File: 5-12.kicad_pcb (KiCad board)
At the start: 2 copper layers, 136 parts, among them SW1 SW_Push, U1 ATmega32U4-AU, Y1 16MHz

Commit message: Partially placed diodes
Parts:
- moved D1 258.6 mm to (28.6, 83.3), turned to 90 degrees
- moved D2 257.8 mm to (29.4, 102.4), turned to 90 degrees
- moved D3 239.4 mm to (29.4, 121.5), turned to 90 degrees
- moved D4 227.8 mm to (29.4, 140.6), turned to 90 degrees
- moved D7 226.8 mm to (48.4, 102.4), turned to 90 degrees
- moved D11 223.2 mm to (67.5, 83.3), turned to 90 degrees
- moved D6 218.9 mm to (48.4, 83.3), turned to 90 degrees
- moved D5 214.1 mm to (29.4, 159.6), turned to 90 degrees
- moved F1 206.3 mm to (162.7, 57.9)
- moved D16 205.3 mm to (86.5, 83.3), turned to 90 degrees
- moved D26 202.8 mm to (124.6, 83.3), turned to 90 degrees
- moved USB1 200.6 mm to (143.5, 55.5), turned to 270 degrees
- moved D21 197.7 mm to (105.6, 83.3), turned to 90 degrees
- moved D13 185.0 mm to (67.5, 121.5), turned to 90 degrees
- moved D27 177.6 mm to (124.6, 102.5), turned to 90 degrees
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
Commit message: swapped MX footprints for NOLED version
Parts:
- MX1, MX10, MX11, MX12, MX13, MX14, MX15, MX16, MX17, MX18, MX19, MX2, MX20, MX21, MX22, MX23, MX24, MX25, MX26, MX27, MX28, MX29, MX3, MX31, MX32, MX33, MX34, MX36, MX37, MX38, MX39, MX4, MX40, MX41, MX42, MX43, MX44, MX45, MX46, MX47, MX48, MX49, MX5, MX50, MX51, MX52, MX53, MX54, MX55, MX56, MX57, MX58, MX59, MX6, MX60, MX7, MX8, MX9: footprint MX_Only:MXOnly-1U -> MX_Only:MXOnly-1U-NoLED
- MX30, MX35: footprint MX_Only:MXOnly-2U -> MX_Only:MXOnly-2U-ReversedStabilizers-NoLED

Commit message: initial, normal diode placement done
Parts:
- moved D12 213.0 mm to (67.5, 102.3), turned to 90 degrees
- moved D56 211.5 mm to (277.0, 83.4), turned to 90 degrees
- moved D51 209.3 mm to (258.0, 83.4), turned to 90 degrees
- moved D57 200.5 mm to (277.0, 102.5), turned to 90 degrees
- moved D58 195.4 mm to (277.0, 121.5), turned to 90 degrees
- moved D17 193.7 mm to (86.5, 102.5), turned to 90 degrees
- moved D41 190.8 mm to (219.9, 83.4), turned to 90 degrees
- moved D59 189.2 mm to (277.0, 140.5), turned to 90 degrees
- moved D18 187.4 mm to (86.5, 121.4), turned to 90 degrees
- moved D22 184.3 mm to (105.6, 102.5), turned to 90 degrees
- moved D31 182.8 mm to (181.8, 83.3), turned to 90 degrees
- moved D42 182.6 mm to (219.9, 102.5), turned to 90 degrees
- moved D46 181.7 mm to (238.9, 83.4), turned to 90 degrees
- moved D8 176.7 mm to (48.4, 121.4), turned to 90 degrees
- moved D48 172.9 mm to (238.9, 121.5), turned to 90 degrees
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
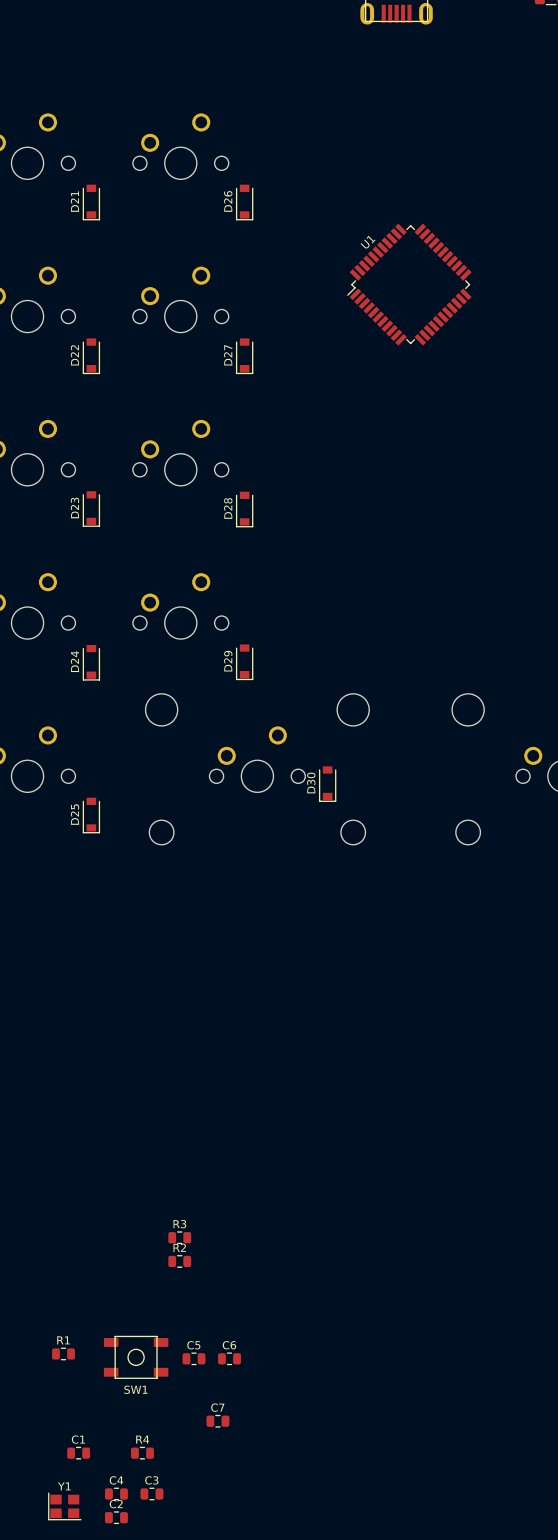
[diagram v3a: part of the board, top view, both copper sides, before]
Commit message: Completed initial layout for MCU zone
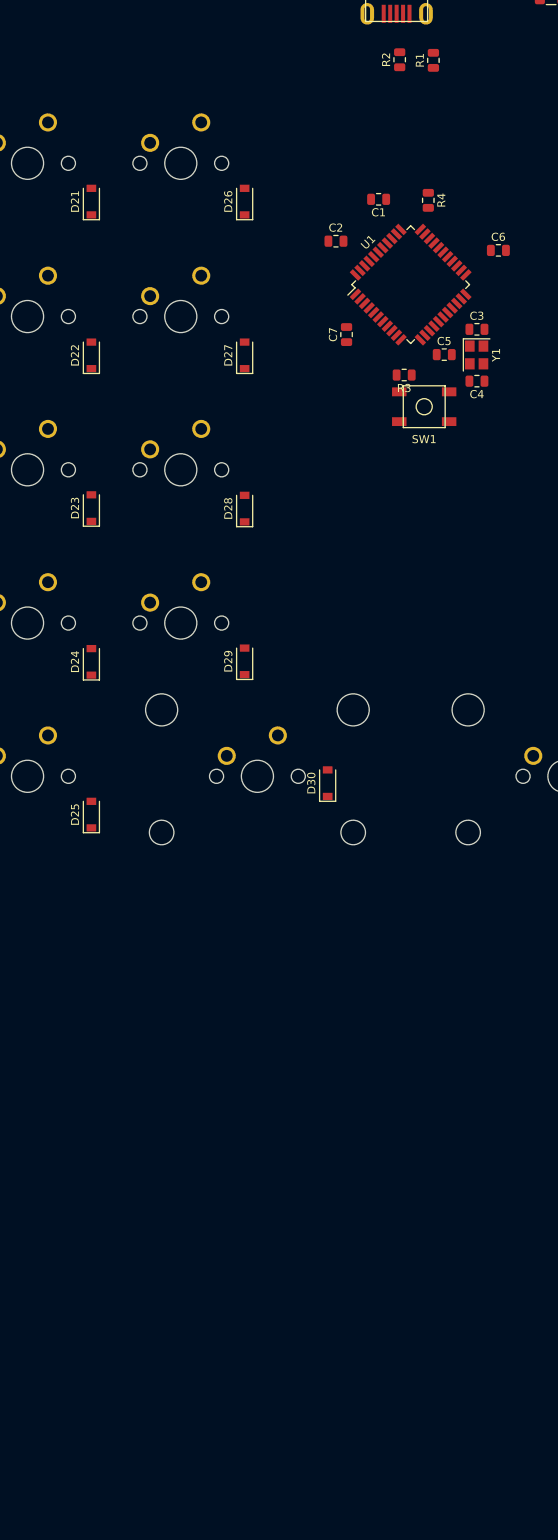
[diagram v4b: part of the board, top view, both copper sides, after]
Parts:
- moved R1 167.2 mm to (148.1, 65.8), turned to 90 degrees
- moved C2 161.0 mm to (136.0, 88.3)
- moved C1 160.3 mm to (141.3, 83.1), turned to 180 degrees
- moved R4 159.7 mm to (147.4, 83.2), turned to 270 degrees
- moved Y1 152.0 mm to (153.5, 102.4), turned to 270 degrees
- moved R2 151.9 mm to (143.9, 65.7), turned to 90 degrees
- moved C3 150.3 mm to (153.5, 99.2)
- moved C4 145.4 mm to (153.5, 105.7), turned to 180 degrees
- moved C6 141.8 mm to (156.2, 89.4)
- moved C7 136.0 mm to (137.3, 99.9), turned to 90 degrees
- moved C5 128.6 mm to (149.4, 102.4)
- moved SW1 123.5 mm to (146.9, 108.8)
- moved R3 110.8 mm to (144.4, 104.9), turned to 180 degrees

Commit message: Initial usb placement
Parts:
- moved R1 17.5 mm to (165.5, 66.6)
- moved R2 17.5 mm to (161.4, 66.5)
- moved USB1 15.3 mm to (145.7, 70.6)
- moved F1 4.36 mm to (159.7, 61.1)
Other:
- board outline added: 266.7 x 95.2 mm
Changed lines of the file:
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@@
   (general
     (thickness 1.6)
-    (drawings 0)
+    (drawings 8)
     (tracks 0)
     (zones 0)
@@
   )
   (module random-keyboard-parts:Molex-0548190589 (layer F.Cu)
-    (at 143.51 55.499 270)
+    (at 145.70625 70.64375 270)
     (attr smd)
     (fp_text reference USB1 (at 2.032 0) (layer F.SilkS)
@@
   )
   (module Resistor_SMD:R_0805_2012Metric (layer F.Cu)
-    (at 143.891 65.7075 90)
+    (at 161.3535 66.50125 90)
     (descr "Resistor SMD 0805 (2012 Metric), square (rectangular) end terminal, IPC_7351 nominal, (Body size source: https://docs.google.com/spreadsheets/d/1BsfQQcO9C6DZCsRaXUlFlo91Tg2WpOkGARC1WS5S8t0/edit?usp=sharing), generated with kicad-footprint-generator")
     (tags resistor)
@@
   )
   (module Resistor_SMD:R_0805_2012Metric (layer F.Cu)
-    (at 148.082 65.786 90)
+    (at 165.5445 66.57975 90)
     (descr "Resistor SMD 0805 (2012 Metric), square (rectangular) end terminal, IPC_7351 nominal, (Body size source: https://docs.google.com/spreadsheets/d/1BsfQQcO9C6DZCsRaXUlFlo91Tg2WpOkGARC1WS5S8t0/edit?usp=sharing), generated with kicad-footprint-generator")
     (tags resistor)
@@
   )
   (module Fuse:Fuse_1206_3216Metric (layer F.Cu)
-    (at 162.71875 57.94375)
+    (at 159.73125 61.11875)
     (descr "Fuse SMD 1206 (3216 Metric), square (rectangular) end terminal, IPC_7351 nominal, (Body size source: http://www.tortai-tech.com/upload/download/2011102023233369053.pdf), generated with kicad-footprint-generator")
     (tags resistor)
@@
     )
   )
+  (gr_line (start 11.90625 161.925) (end 11.90625 71.4375) (layer Edge.Cuts) (width 0.05))
+  (gr_line (start 276.225 164.30625) (end 14.2875 164.30625) (layer Edge.Cuts) (width 0.05))
+  (gr_line (start 278.60625 71.4375) (end 278.60625 161.925) (layer Edge.Cuts) (width 0.05))
+  (gr_line (start 14.2875 69.05625) (end 276.225 69.05625) (layer Edge.Cuts) (width 0.05))
+  (gr_arc (start 14.2875 161.925) (end 11.90625 161.925) (angle -90) (layer Edge.Cuts) (width 0.05))
+  (gr_arc (start 14.2875 71.4375) (end 14.2875 69.05625) (angle -90) (layer Edge.Cuts) (width 0.05))
+  (gr_arc (start 276.225 161.925) (end 276.225 164.30625) (angle -90) (layer Edge.Cuts) (width 0.05))
+  (gr_arc (start 276.225 71.4375) (end 278.60625 71.4375) (angle -90) (layer Edge.Cuts) (width 0.05))
 )

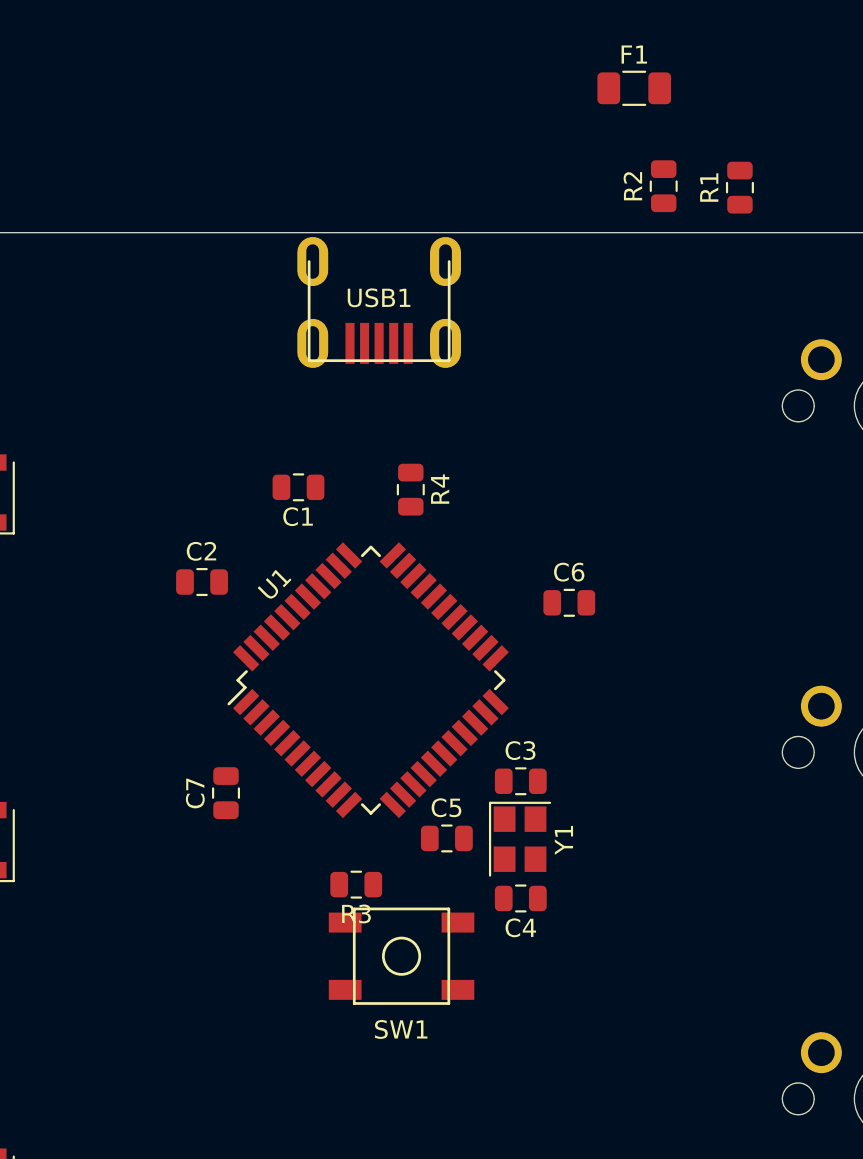
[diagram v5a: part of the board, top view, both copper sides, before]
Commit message: initial placement of usb components, rotation of mcu, replacement and adjustment of MCU group
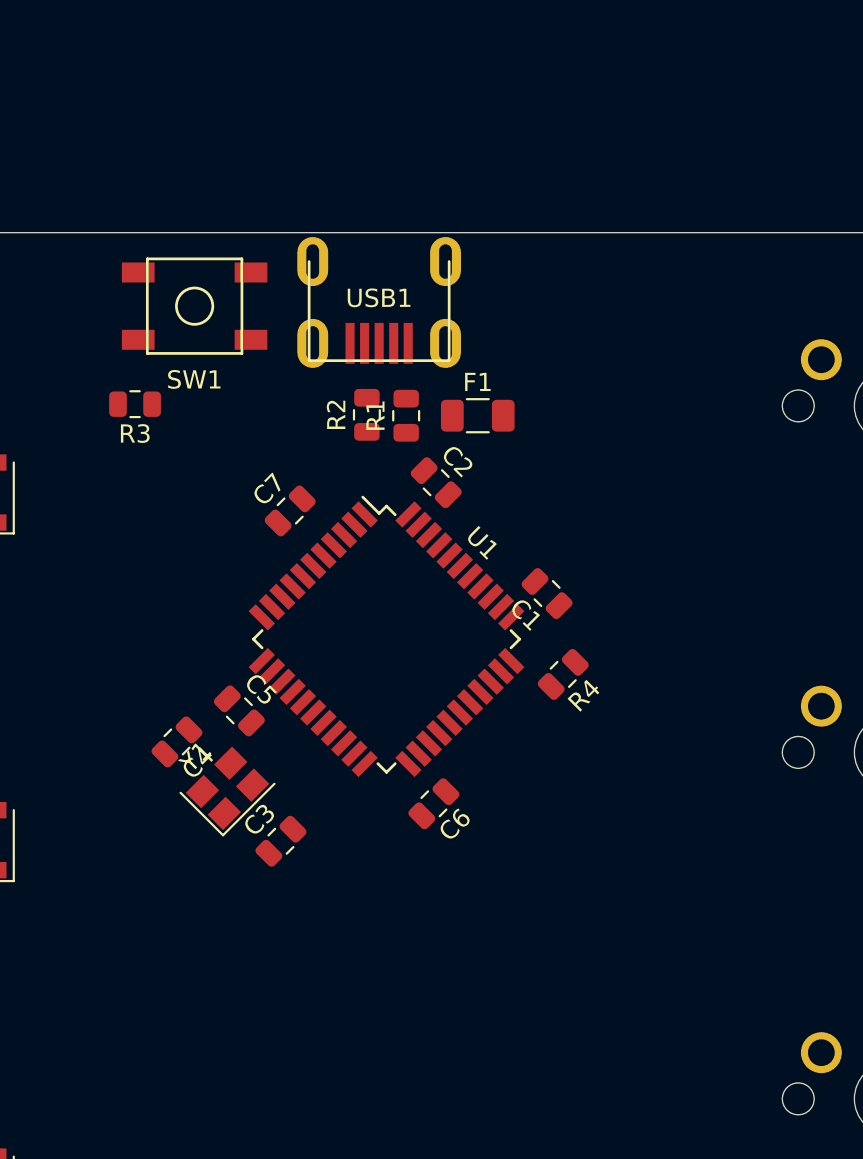
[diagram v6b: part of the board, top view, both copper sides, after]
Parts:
- moved SW1 37.5 mm to (135.6, 73.1)
- moved R3 29.1 mm to (132.3, 78.5)
- moved R1 22.2 mm to (147.2, 79.1)
- moved C4 20.8 mm to (134.6, 97.1), turned to 225 degrees
- moved R2 20.6 mm to (145.0, 79.1)
- moved F1 20.0 mm to (151.1, 79.1)
- moved Y1 16.3 mm to (137.4, 99.6), turned to 45 degrees
- moved C7 15.9 mm to (140.8, 84.4), turned to 45 degrees
- moved C1 14.9 mm to (154.9, 88.9), turned to 135 degrees
- moved C2 14.0 mm to (148.8, 82.8), turned to 315 degrees
- moved C3 13.6 mm to (140.3, 102.5), turned to 45 degrees
- moved C5 13.4 mm to (138.0, 95.3), turned to 315 degrees
- moved C6 13.3 mm to (148.7, 100.5), turned to 225 degrees
- moved R4 13.2 mm to (155.8, 93.3), turned to 225 degrees
- moved U1 2.41 mm to (146.1, 91.4), turned to 315 degrees

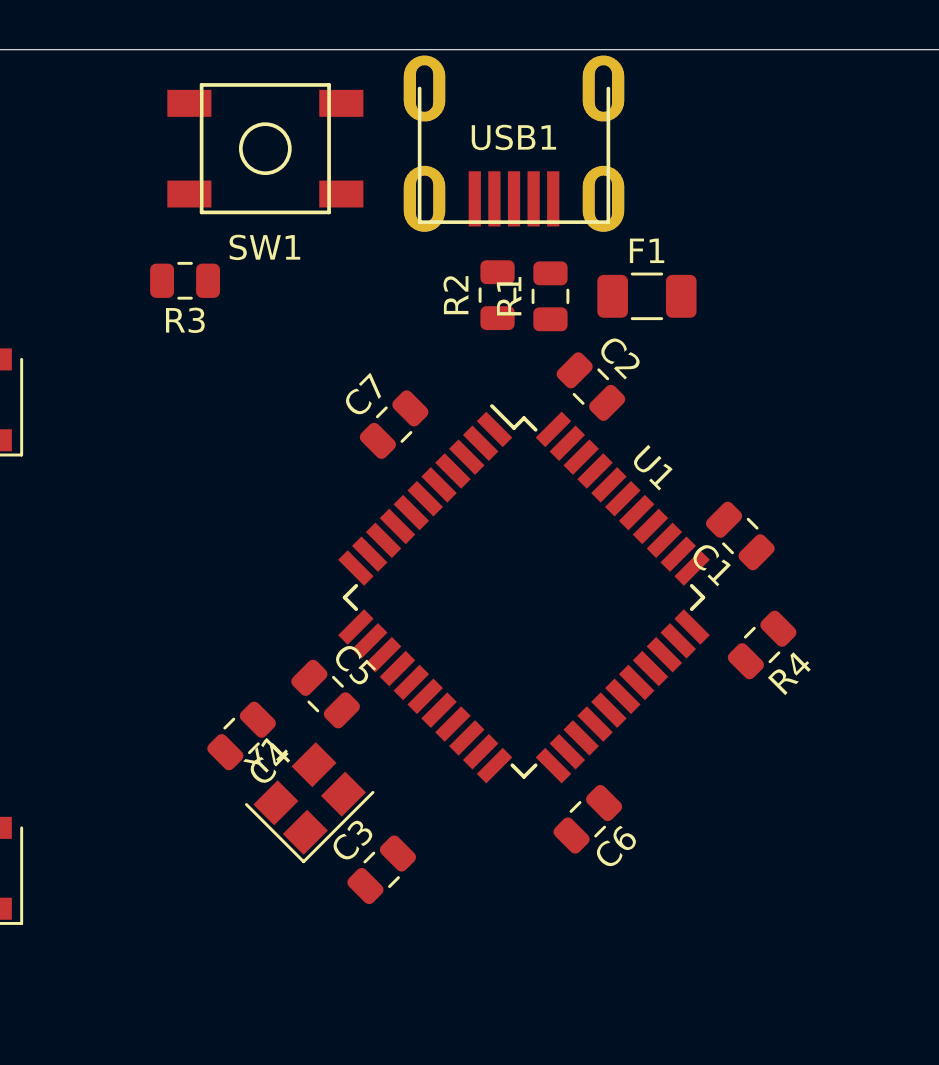
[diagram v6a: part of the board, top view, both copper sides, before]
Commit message: Wired mcu and usb
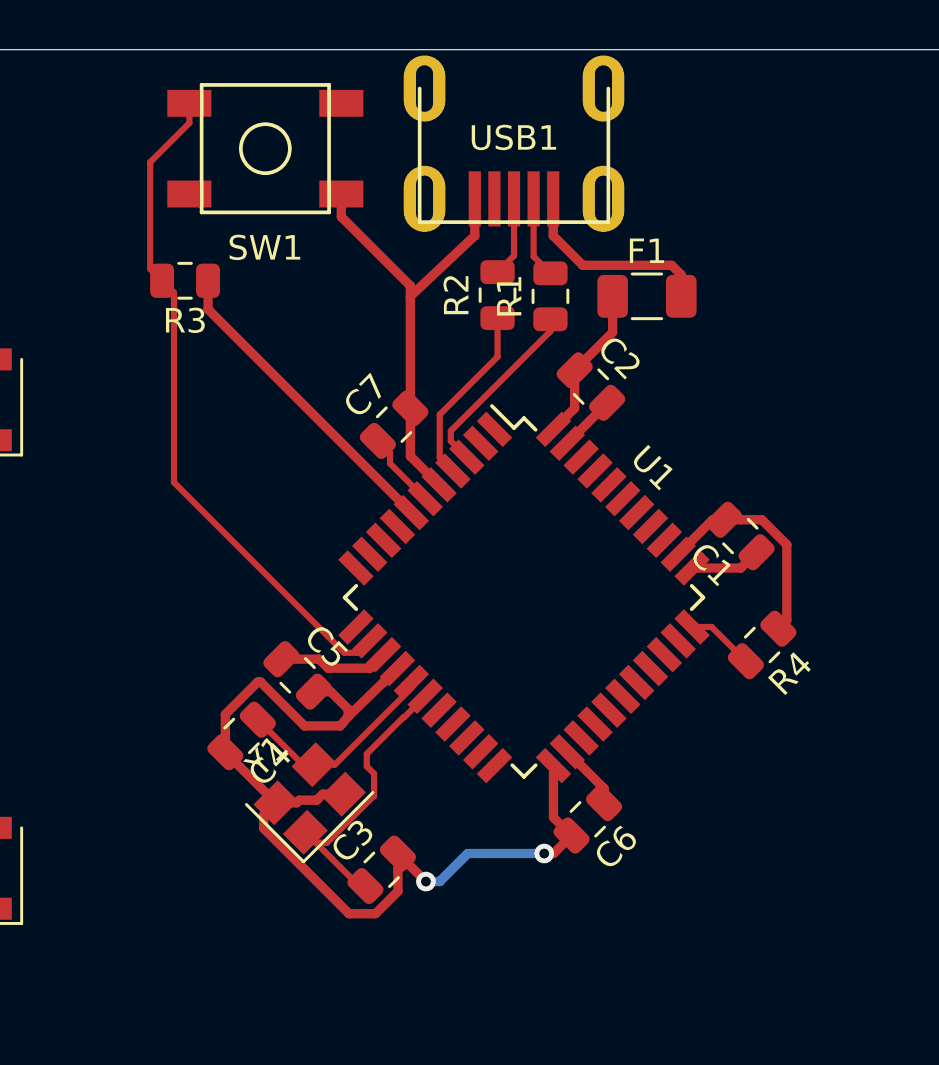
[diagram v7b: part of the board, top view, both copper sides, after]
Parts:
- moved C5 1.37 mm to (136.9, 94.6)
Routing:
- net GND: track 0.00 -> 71.2 mm, vias 0 -> 2
- net +5V: track 0.00 -> 29.5 mm
- net Net-(R3-Pad2): track 0.00 -> 27.6 mm
- net Net-(C3-Pad1): track 0.00 -> 12.3 mm
- net Net-(C4-Pad1): track 0.00 -> 8.55 mm
- net VCC: track 0.00 -> 8.27 mm
- net Net-(R1-Pad1): track 0.00 -> 7.58 mm
- net Net-(R2-Pad1): track 0.00 -> 7.44 mm
- net D-: track 0.00 -> 3.32 mm
- net D+: track 0.00 -> 3.27 mm
- net Net-(C7-Pad1): track 0.00 -> 3.16 mm
- net Net-(R4-Pad2): track 0.00 -> 2.77 mm
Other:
- net class Default: trace_width 0.25 -> 0.254
- net class Power added: clearance 0.2, trace_width 0.381, via_dia 0.8, via_drill 0.4
